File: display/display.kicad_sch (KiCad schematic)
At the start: 18 parts, among them J1 Raspberry Pi

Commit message: Update to kicad 8
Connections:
- net dE: now also XA1.SDA; no longer XA1.D22
- net dF: now also XA1.SCL; no longer XA1.D23
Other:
- moved on the sheet: J1, LS0, LS1, LS10, LS11, LS12, LS13, LS14, LS15, LS2, LS3, LS4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

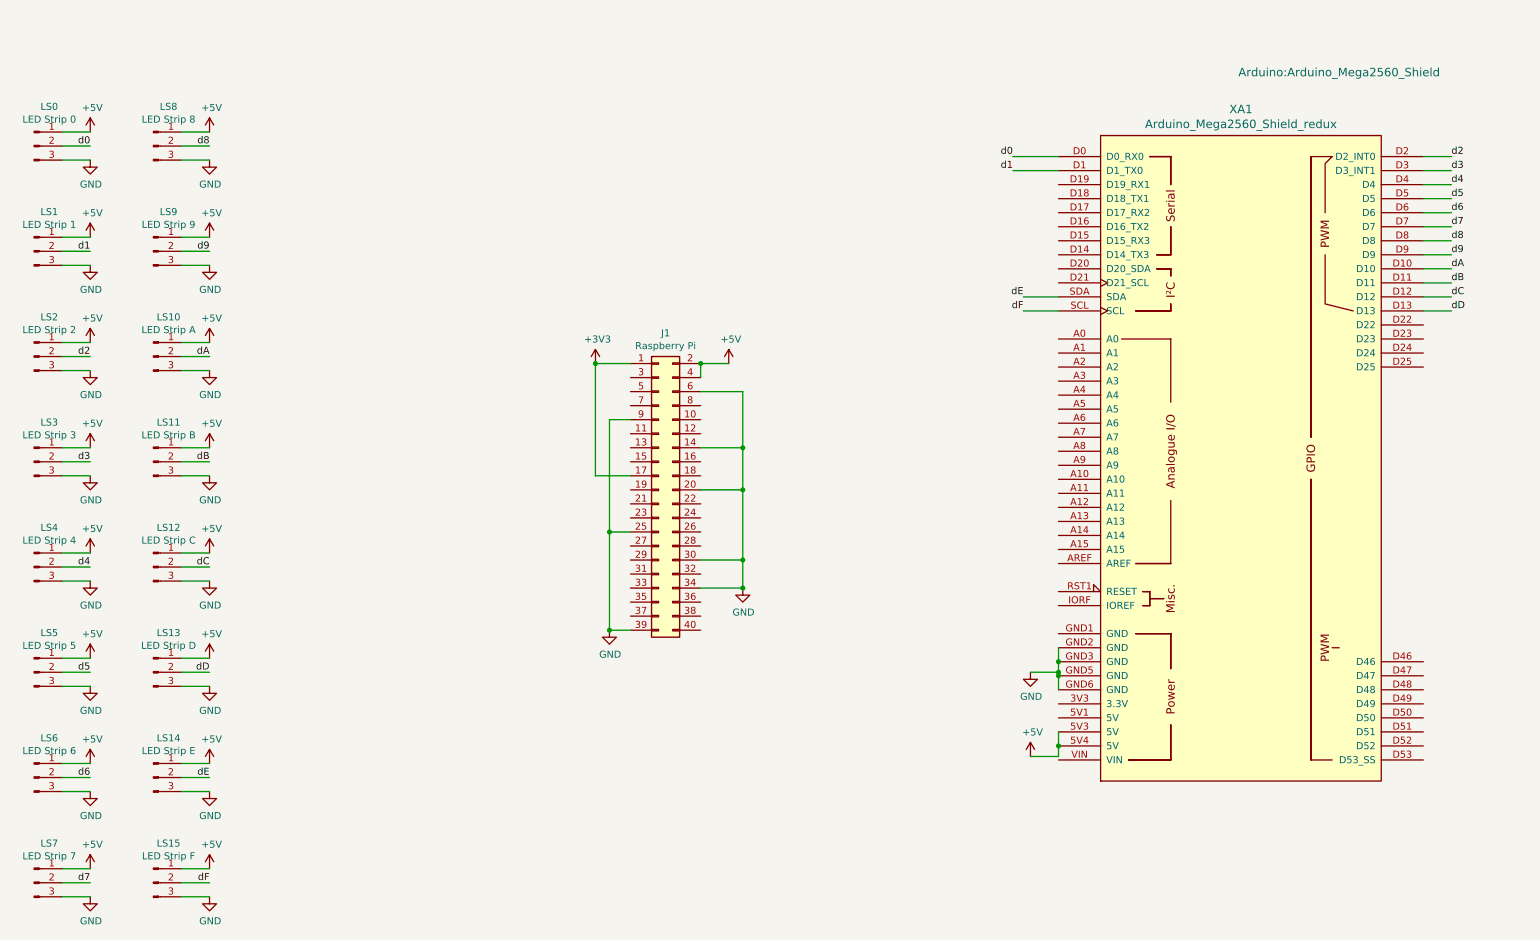
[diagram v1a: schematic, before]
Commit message: Add SPI and SYNC pins
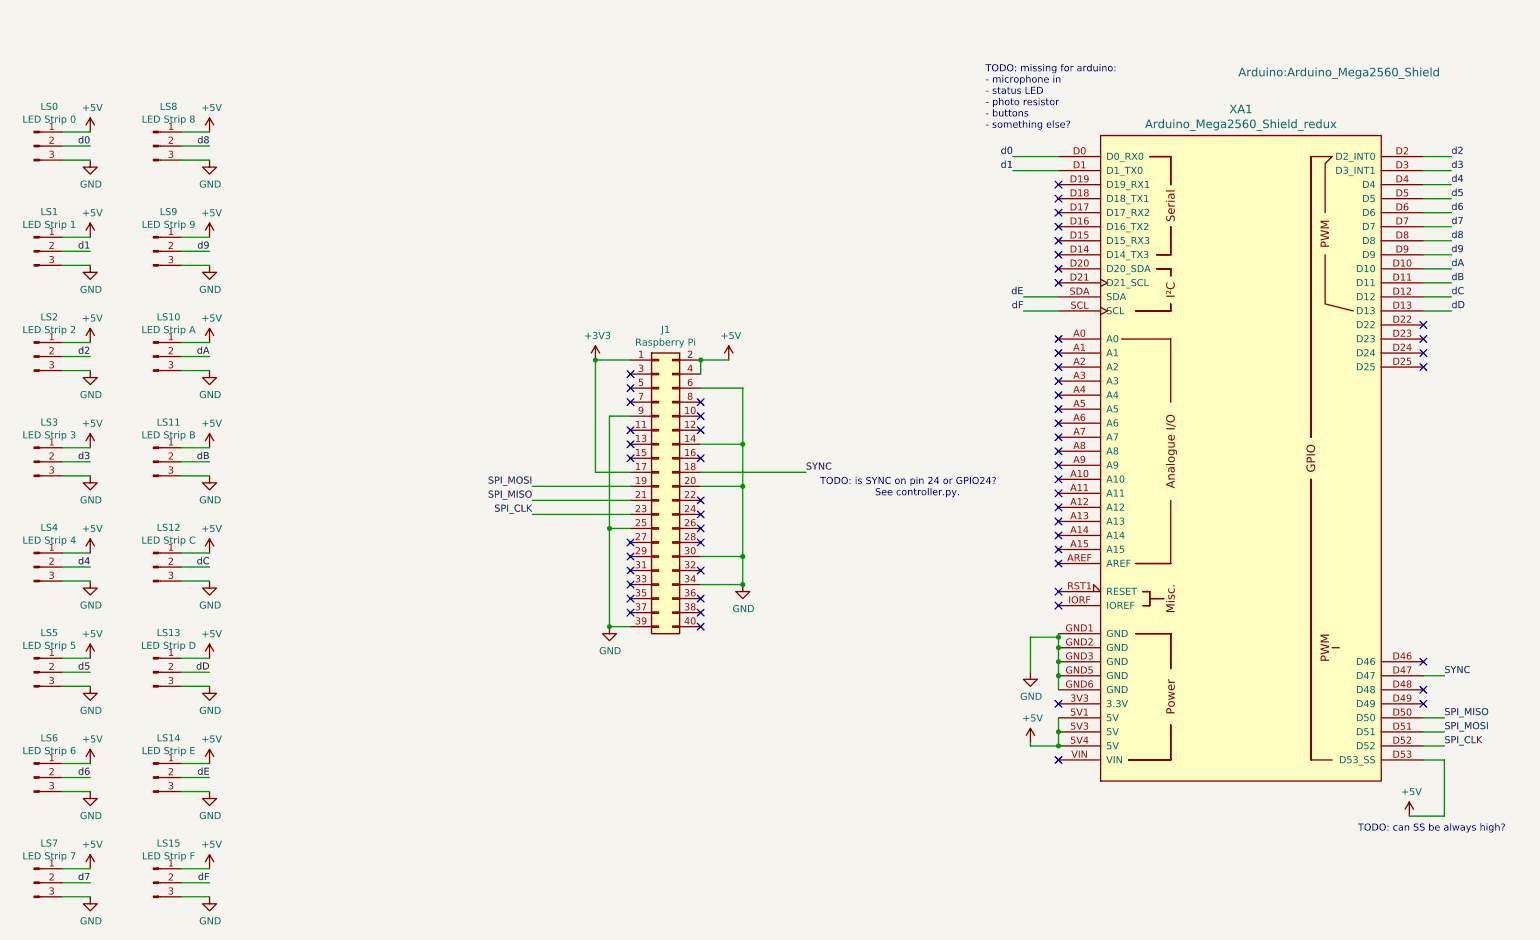
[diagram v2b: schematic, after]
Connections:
- net +5V: now also XA1.5V1 (5V), XA1.D53 (D53_SS)
- net GND: now also XA1.GND1 (GND)
- net SYNC: now reaches XA1.D47
- net SYNC: now also J1.18 (Pin_18)
- net SPI_MISO: now reaches XA1.D50
- net SPI_MISO: now also J1.21 (Pin_21)
- net SPI_MOSI: now reaches XA1.D51
- net SPI_MOSI: now also J1.19 (Pin_19)
- net SPI_CLK: now reaches XA1.D52
- net SPI_CLK: now also J1.23 (Pin_23)
- no-connect marks 0 -> 60
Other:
- note added: "TODO: can SS be always high?"
- note added: "TODO: is SYNC on pin 24 or GPIO24? See controller.py."
- note added: "TODO: missing for arduino: - microphone in - status LED - photo resistor - buttons - something else?"
- moved on the sheet: J1
